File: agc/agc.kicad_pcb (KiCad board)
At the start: 2 copper layers, 72.4 x 59.1 mm, 63 parts, among them J5 SIL10, K1 TR, K10 HVMON, K11 HVMON, K2 TR, K3 VIN, K4 VOUT_TR, K5 TR, K6 TR, K7 HVMON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

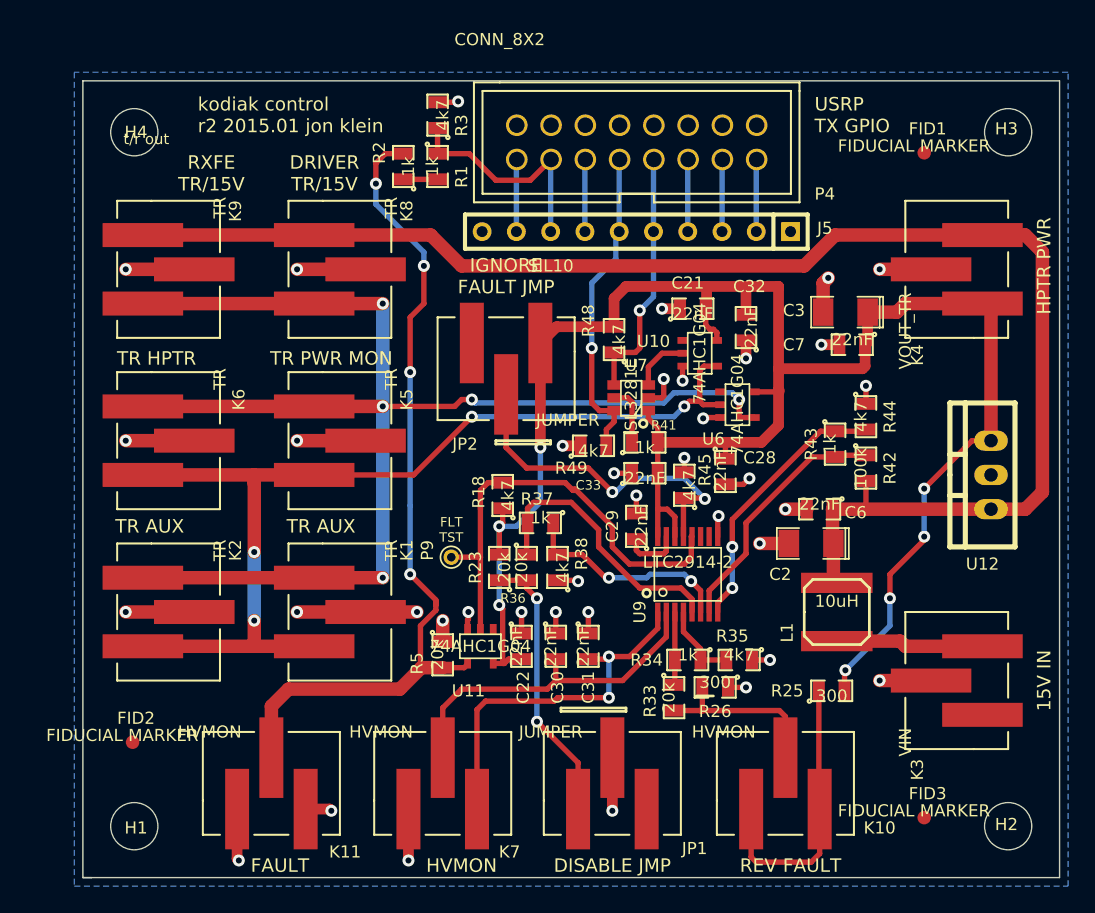
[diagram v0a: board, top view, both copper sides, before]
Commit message: DFM changes to boards - added fiducial markers and increase paste clearance
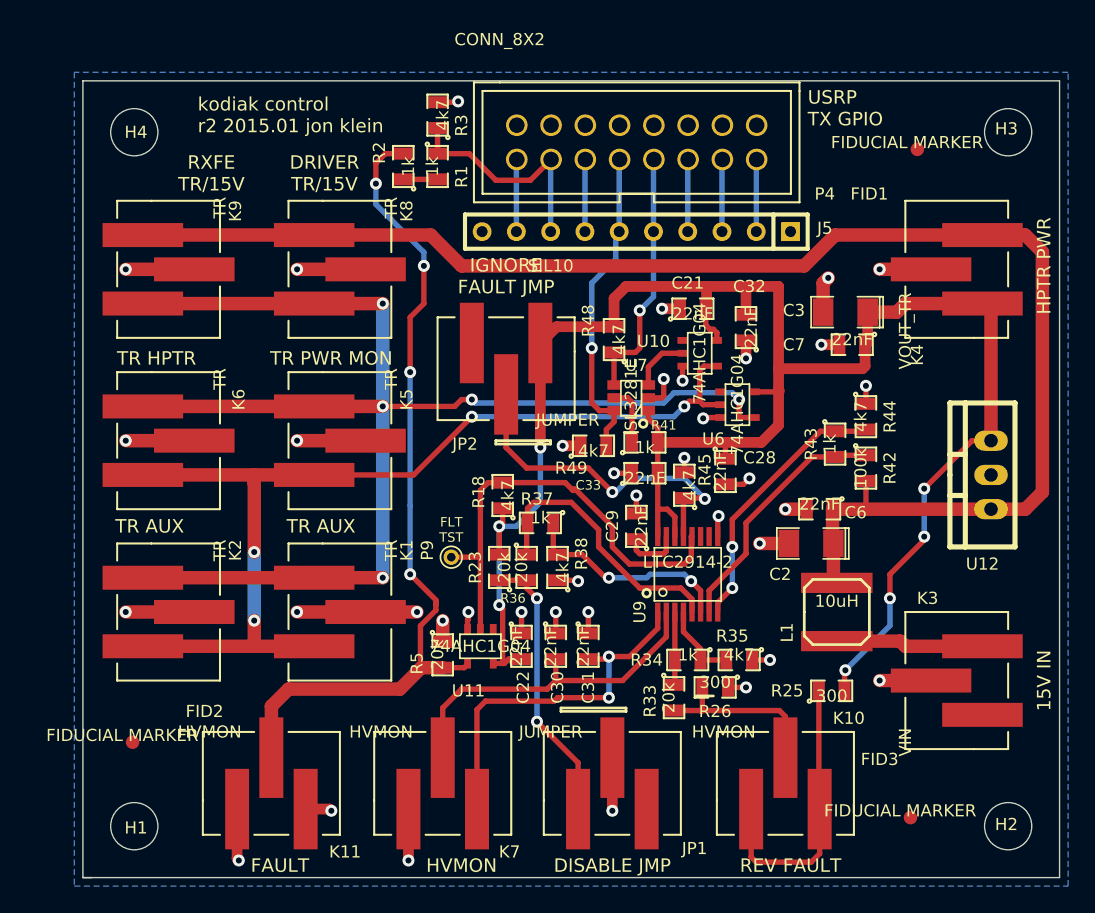
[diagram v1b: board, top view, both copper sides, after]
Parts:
- moved FID3 1.02 mm to (94.2, 108.0)
- moved FID1 0.57 mm to (94.7, 58.4)
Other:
- board text removed: "t/r out"
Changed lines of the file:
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@@
     (links 134)
     (no_connects 0)
-    (area 32.842999 53.289999 105.333001 112.445001)
+    (area 29.610786 32.23 109.380501 114.48376)
     (thickness 1.6)
-    (drawings 36)
+    (drawings 35)
     (tracks 459)
     (zones 0)
@@
     (visible_elements FFFEFF7F)
     (pcbplotparams
-      (layerselection 284196871)
+      (layerselection 284721153)
       (usegerberextensions true)
       (excludeedgelayer true)
@@
   (module localconn:3-647166-3 (layer F.Cu)
     (at 97.663 97.79 90)
-    (fp_text reference K3 (at -6.604 -2.921 90) (layer F.SilkS)
+    (fp_text reference K3 (at 6.096 -2.159 180) (layer F.SilkS)
       (effects (font (size 0.9 0.9) (thickness 0.175)))
     )
@@
   (module localconn:3-647166-3 (layer F.Cu)
     (at 84.963 105.41)
-    (fp_text reference K10 (at 6.985 3.302) (layer F.SilkS)
+    (fp_text reference K10 (at 4.699 -4.826) (layer F.SilkS)
       (effects (font (size 0.9 0.9) (thickness 0.175)))
     )
@@
   )
   (module sdtransmitter:FID_1MM (layer F.Cu)
-    (at 95.25 58.674)
-    (fp_text reference FID1 (at 0.254 -1.778) (layer F.SilkS)
+    (at 94.742 58.42)
+    (fp_text reference FID1 (at -3.556 3.302) (layer F.SilkS)
       (effects (font (size 0.9 0.9) (thickness 0.175)))
     )
@@
     )
     (pad 1 smd circle (at 0 0) (size 1 1) (layers F.Cu F.Mask)
-      (solder_mask_margin 3))
+      (solder_mask_margin 2))
   )
   (module sdtransmitter:FID_1MM (layer F.Cu)
     (at 36.576 102.362)
-    (fp_text reference FID2 (at 0.254 -1.778) (layer F.SilkS)
+    (fp_text reference FID2 (at 5.334 -2.286) (layer F.SilkS)
       (effects (font (size 0.9 0.9) (thickness 0.175)))
     )
@@
     )
     (pad 1 smd circle (at 0 0) (size 1 1) (layers F.Cu F.Mask)
-      (solder_mask_margin 3))
+      (solder_mask_margin 2))
   )
   (module sdtransmitter:FID_1MM (layer F.Cu)
-    (at 95.25 107.95)
-    (fp_text reference FID3 (at 0.254 -1.778) (layer F.SilkS)
+    (at 94.234 107.95)
+    (fp_text reference FID3 (at -2.286 -4.318) (layer F.SilkS)
       (effects (font (size 0.9 0.9) (thickness 0.175)))
     )
@@
     )
     (pad 1 smd circle (at 0 0) (size 1 1) (layers F.Cu F.Mask)
-      (solder_mask_margin 3))
+      (solder_mask_margin 2))
   )
   (gr_line (start 68.326 99.822) (end 68.326 100.076) (angle 90) (layer F.SilkS) (width 0.2))
@@
     (effects (font (size 1 1) (thickness 0.2)))
   )
-  (gr_text "USRP\nTX GPIO" (at 87.122 55.88) (layer F.SilkS)
+  (gr_text "USRP\nTX GPIO" (at 86.614 55.372) (layer F.SilkS)
     (effects (font (size 1 1) (thickness 0.25)) (justify left))
   )
@@
     (effects (font (size 1 1) (thickness 0.25)) (justify left))
   )
-  (gr_text "t/r out" (at 37.592 57.658) (layer F.SilkS)
-    (effects (font (size 0.8 0.8) (thickness 0.15)))
-  )
   (gr_circle (center 74.422 78.74) (end 74.168 78.613) (layer F.SilkS) (width 0.2))

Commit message: changed all 3 pin headers to molex smd connectors available in tube packaging..
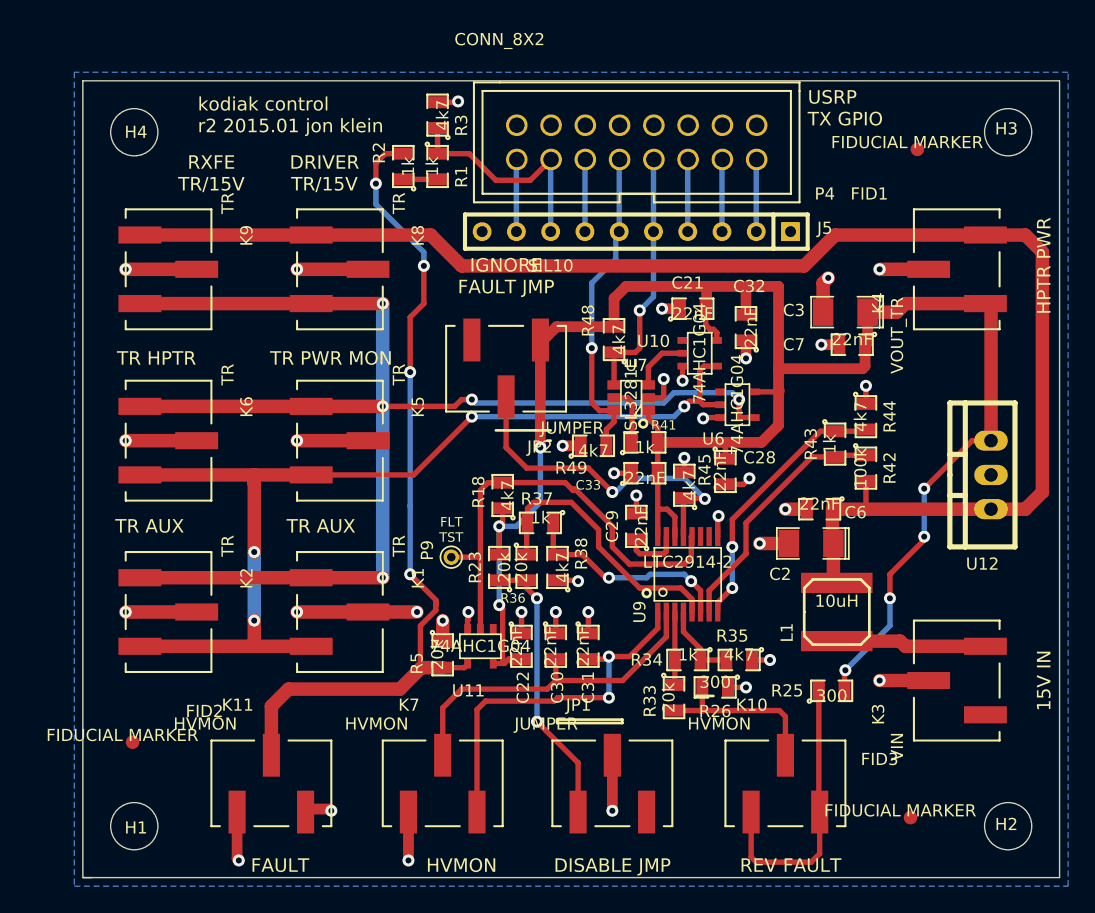
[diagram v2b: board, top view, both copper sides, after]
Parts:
- JP1, JP2, K1, K10, K11, K2, K3, K4, K5, K6, K7, K8, K9: footprint localconn:3-647166-3 -> sdtransmitter:0740991003

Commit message: rearranged high power T/R switch to place all connectors on one side for easier mounting to cases
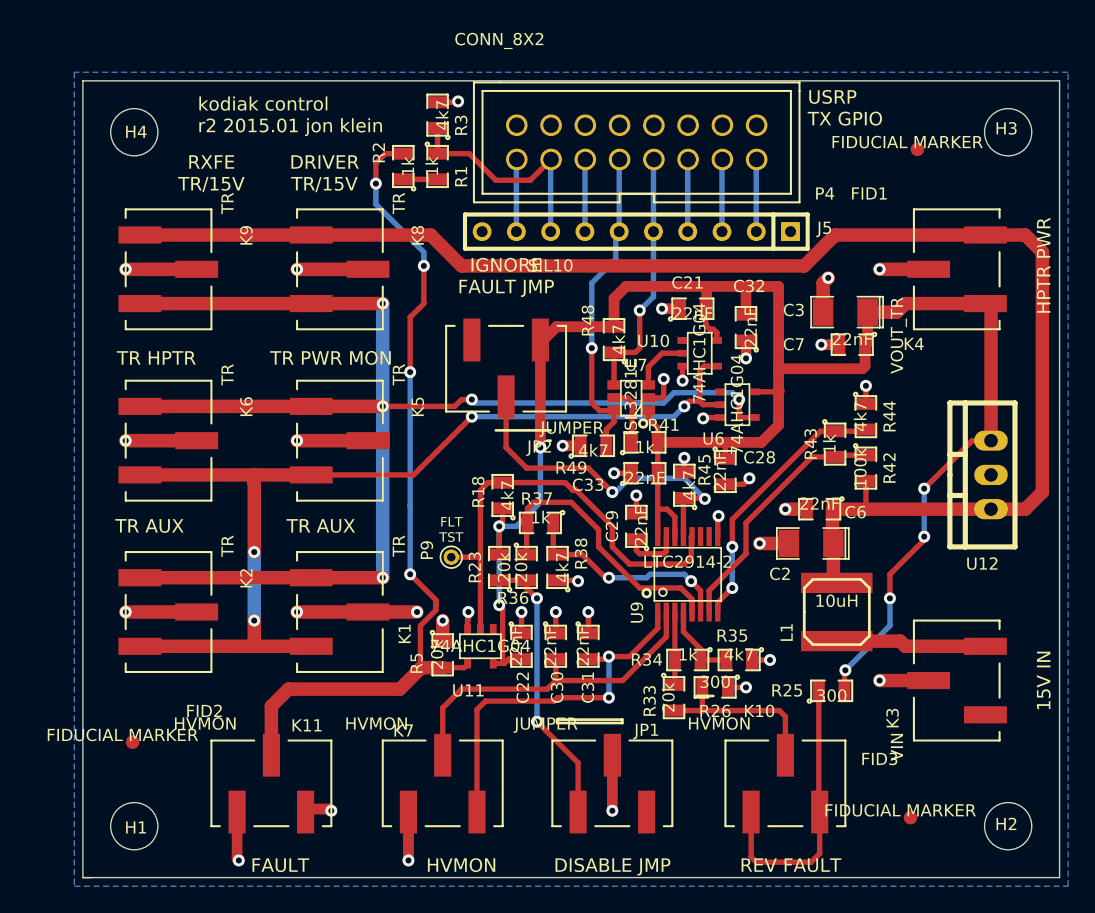
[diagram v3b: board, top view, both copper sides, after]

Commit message: cleaned up silkscreen, moved fiduciary marks at least 4.75ish mm away from board edges
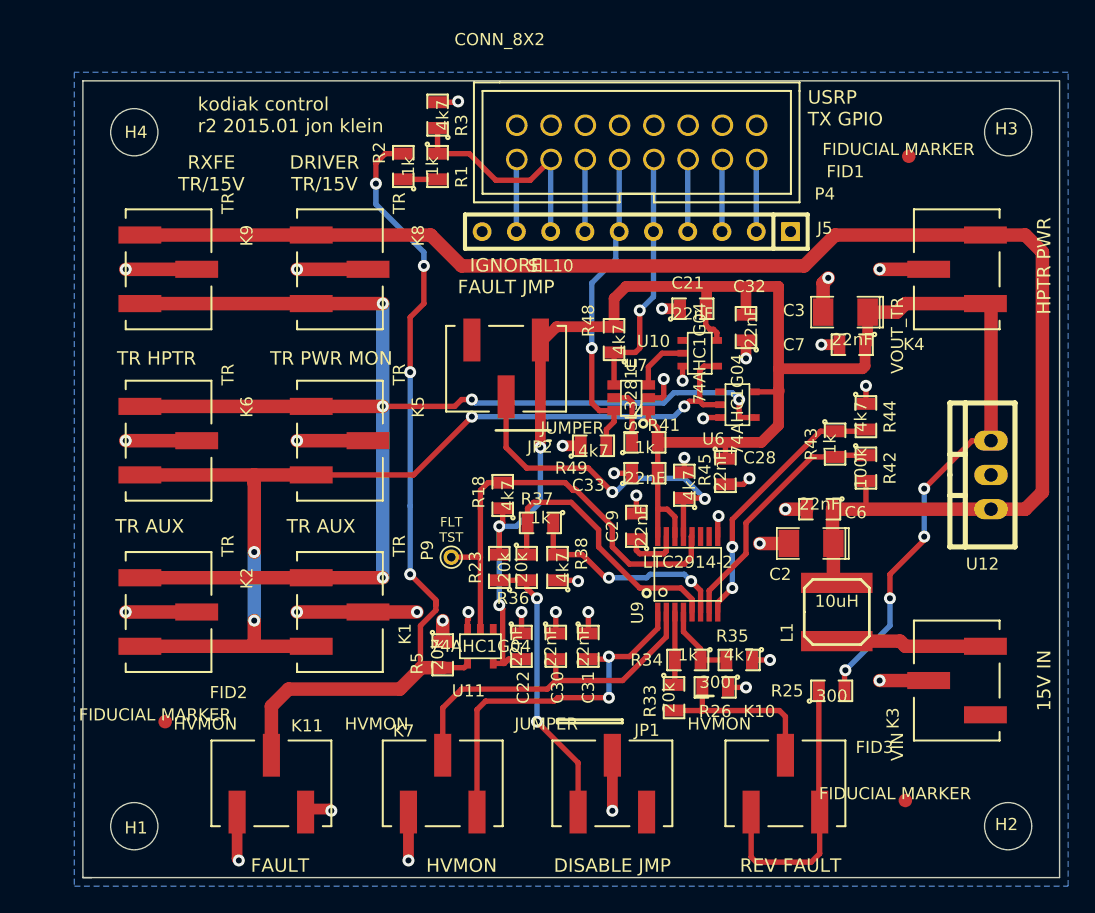
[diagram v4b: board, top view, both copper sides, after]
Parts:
- moved FID2 2.85 mm to (39.0, 100.8)
- moved FID3 1.33 mm to (93.9, 106.7)
- moved FID1 0.81 mm to (94.1, 58.9)

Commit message: DFM changes..
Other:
- outline, holes or cut-outs redrawn

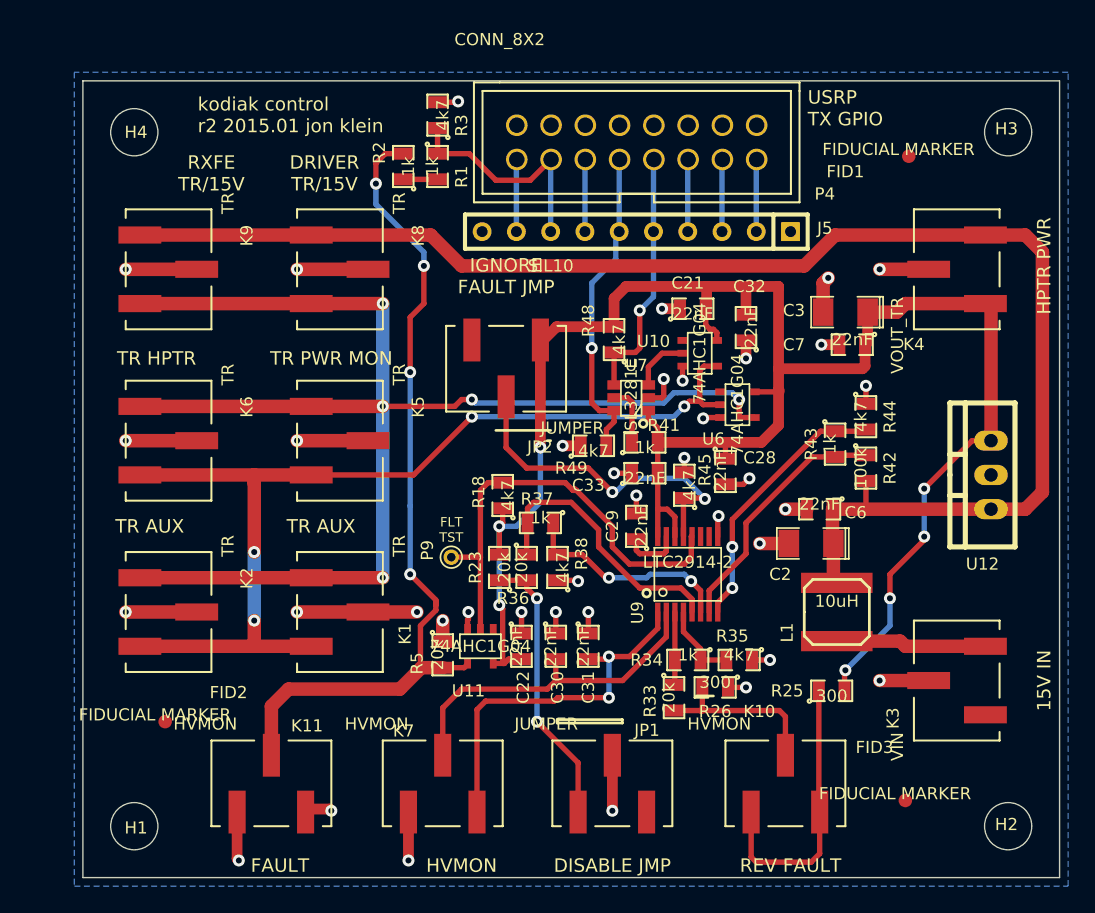
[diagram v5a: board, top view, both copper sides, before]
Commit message: added scripts for using gerbmerge for panelizing boards to reduce assembly costs
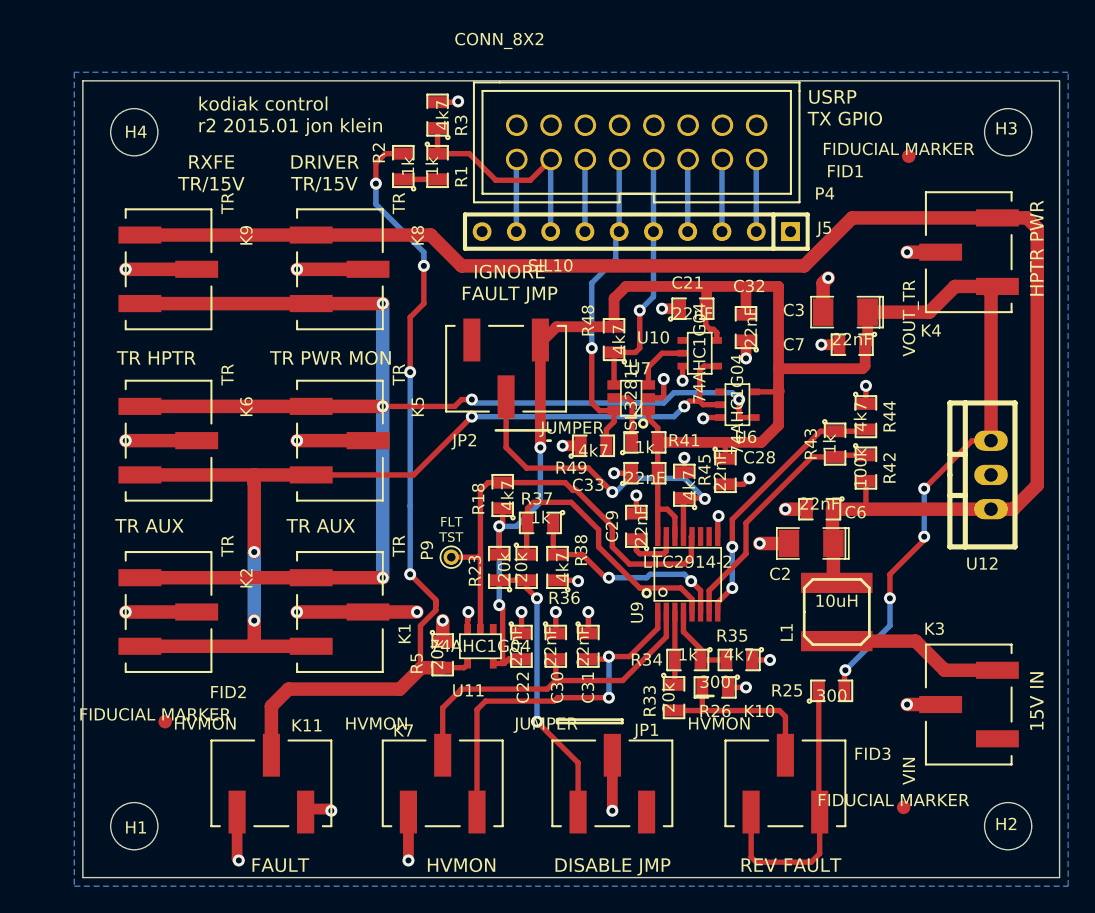
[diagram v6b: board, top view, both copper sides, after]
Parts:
- moved K3 1.99 mm to (98.6, 99.6)
- moved K4 1.55 mm to (98.6, 66.0)
- moved FID3 0.52 mm to (93.7, 107.2)
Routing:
- net GND: track 94.2 -> 91.6 mm
- net +5V: track 148.7 -> 151.2 mm
- net Net-(K3-Pad3): track 11.0 -> 12.8 mm
- net VCC: track 110.6 -> 111.7 mm

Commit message: simplified hptr pin diode biasing.. using a sn75372 might be fun for the next redesign
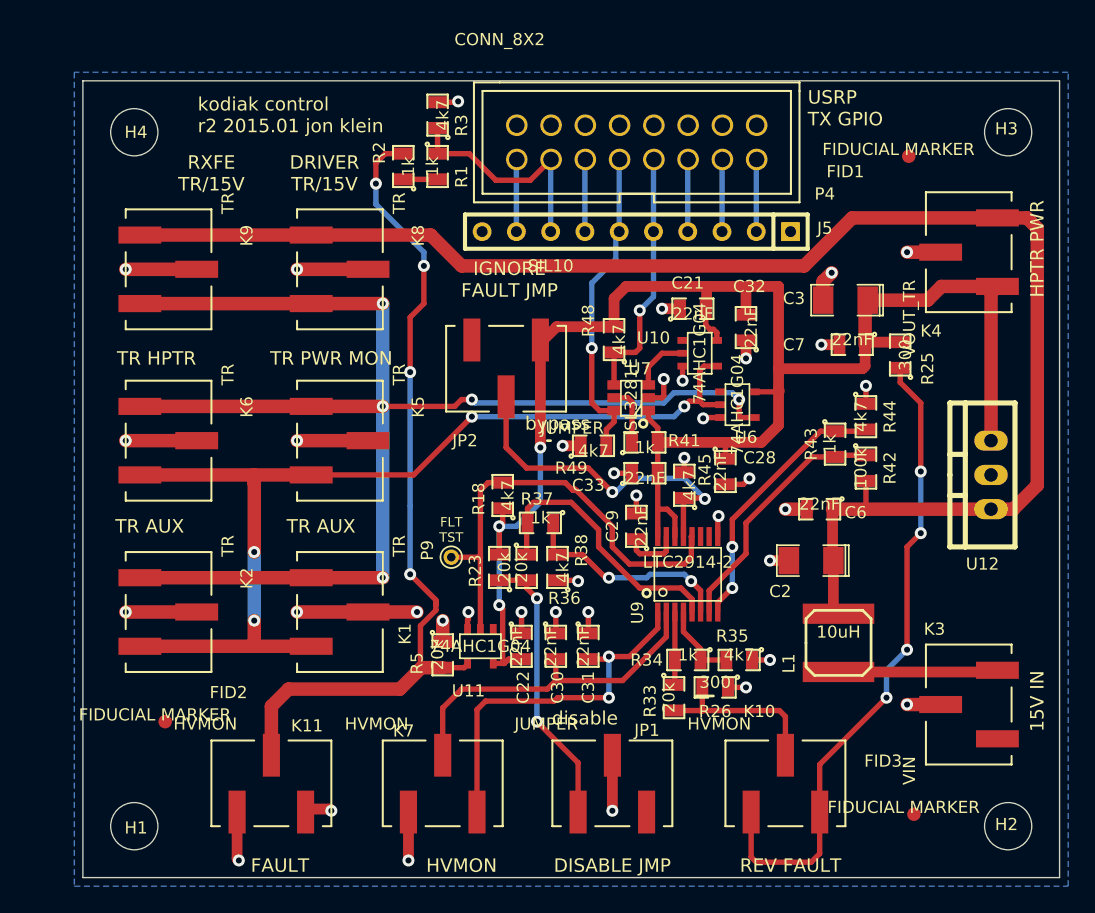
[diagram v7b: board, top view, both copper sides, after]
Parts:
- moved R25 25.4 mm to (93.5, 73.7), turned to 90 degrees
- moved L1 2.29 mm to (88.9, 95.0)
- moved C2 1.27 mm to (86.9, 88.9)
- moved FID3 0.92 mm to (94.5, 107.7)
- moved C3 0.89 mm to (89.4, 69.6)
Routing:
- net Net-(K10-Pad1): track 21.7 -> 49.6 mm, vias 0 -> 4
- net +5V: track 151.2 -> 130.8 mm, vias 7 -> 3
- net VCC: track 111.7 -> 114.0 mm
- net GND: track 91.6 -> 90.4 mm
- net Net-(K3-Pad3): track 12.8 -> 11.8 mm
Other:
- board text added: "bypass"
- board text added: "disable"
